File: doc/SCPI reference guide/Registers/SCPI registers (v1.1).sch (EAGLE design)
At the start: 0 parts

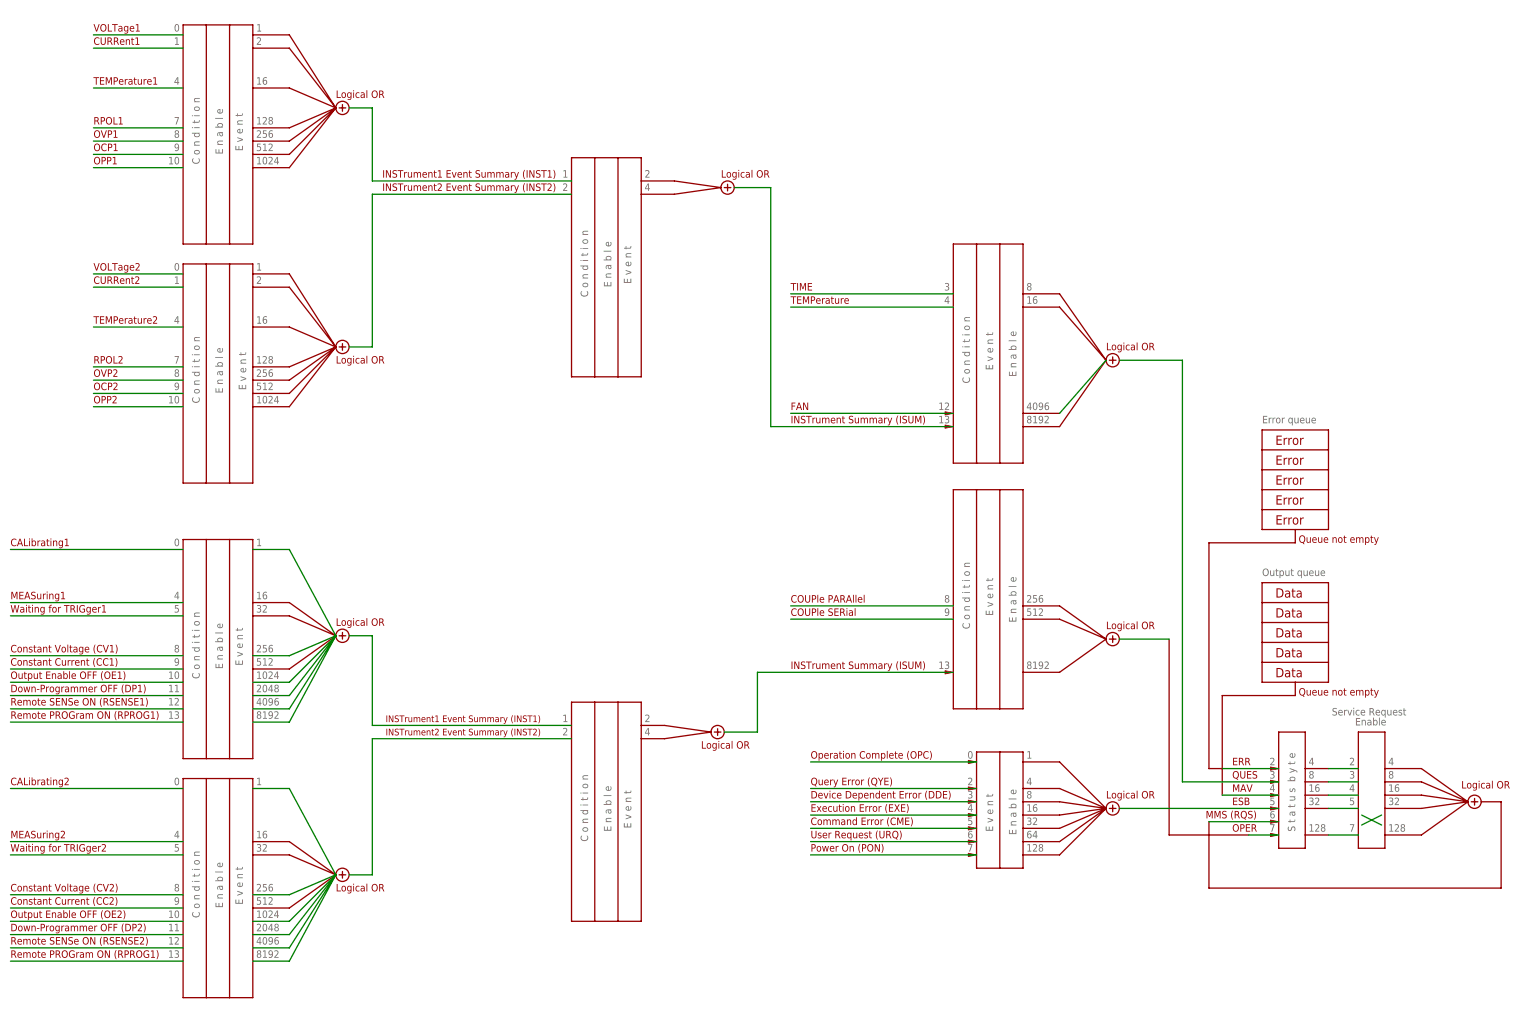
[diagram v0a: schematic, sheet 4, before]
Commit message: SCPI doc update for DLOG
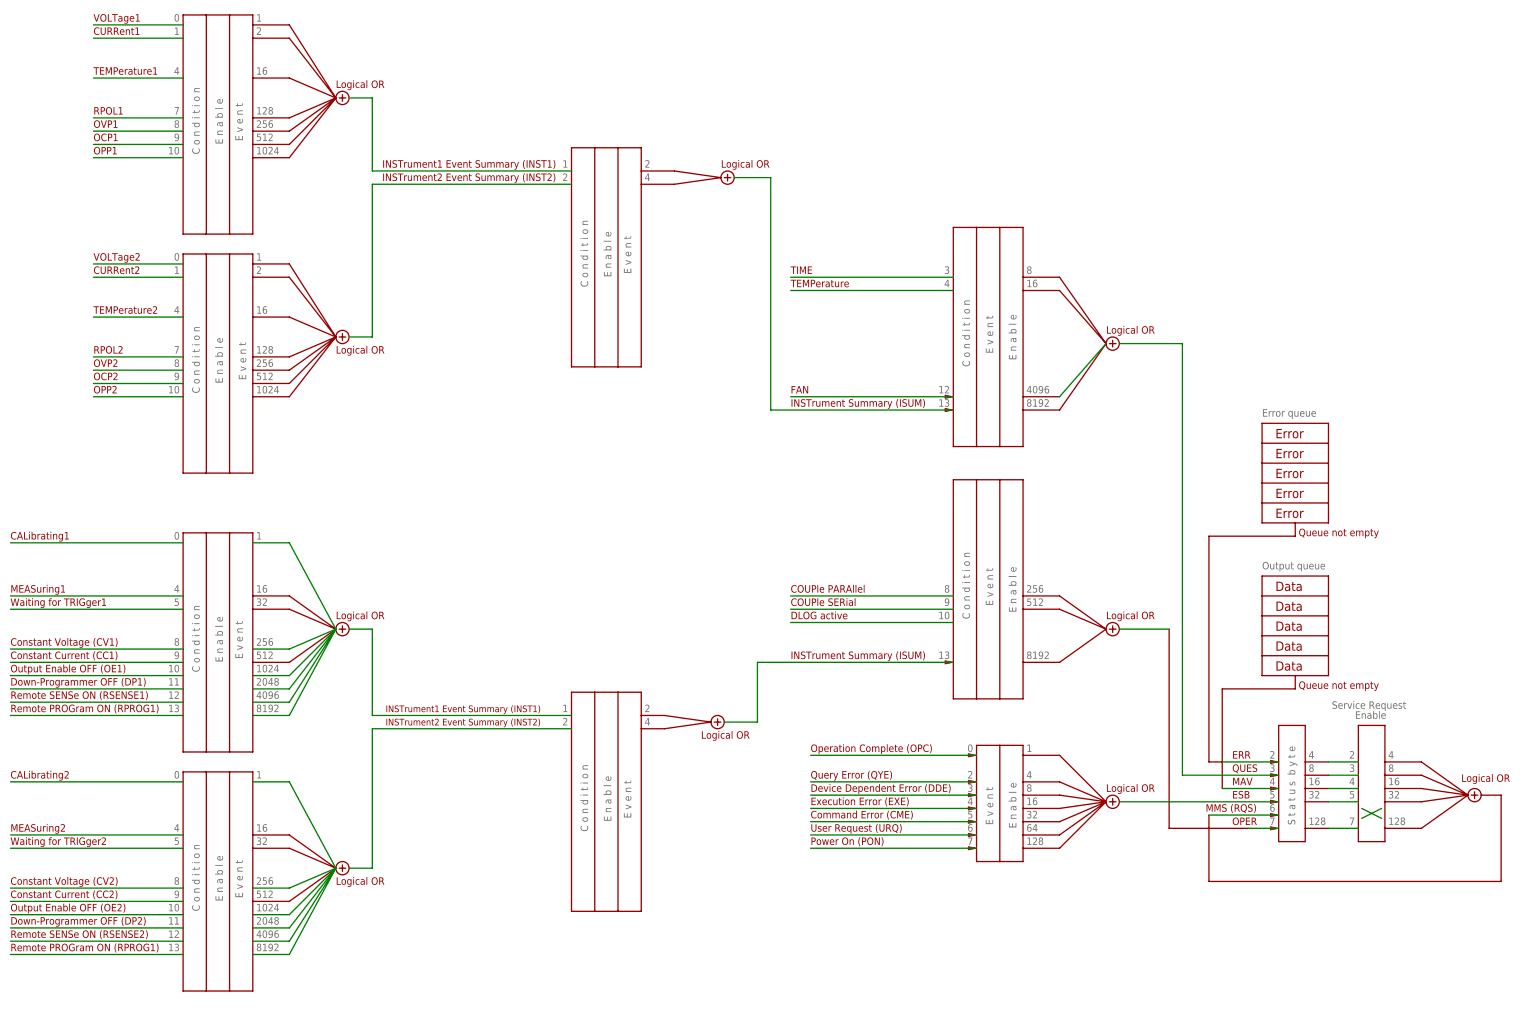
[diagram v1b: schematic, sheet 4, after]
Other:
- note added: "DLOG active"
